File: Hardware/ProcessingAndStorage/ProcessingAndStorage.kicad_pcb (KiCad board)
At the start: 2 copper layers, 85 x 60 mm, 31 parts, among them J1 Micro_SD_Card_Det2, J5 Conn_02x11_Odd_Even, SW2 SW_SPDT_XKB_DMx-xxxx-1, U1 LD1117S50TR_SOT223, U2 ESP-12E, U3 LD1117S50TR_SOT223

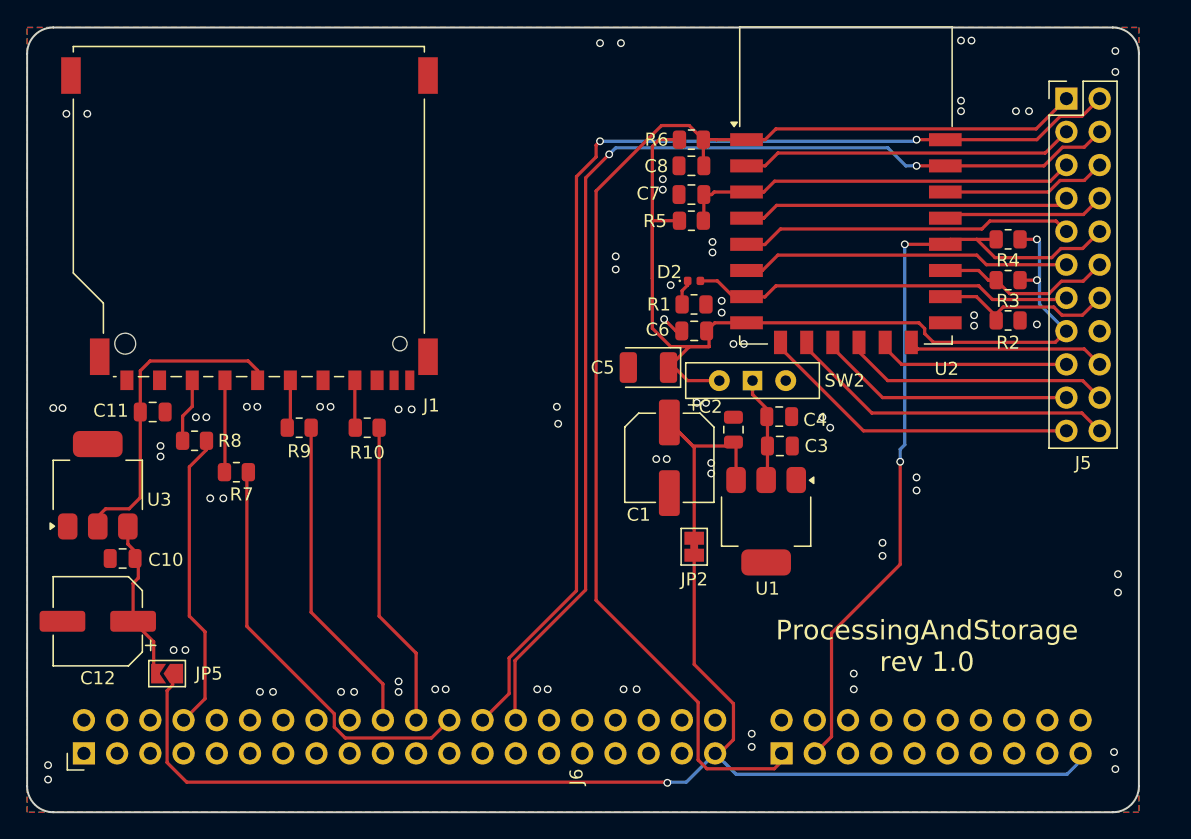
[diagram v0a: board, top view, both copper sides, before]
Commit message: rework CI, make PCB smaller
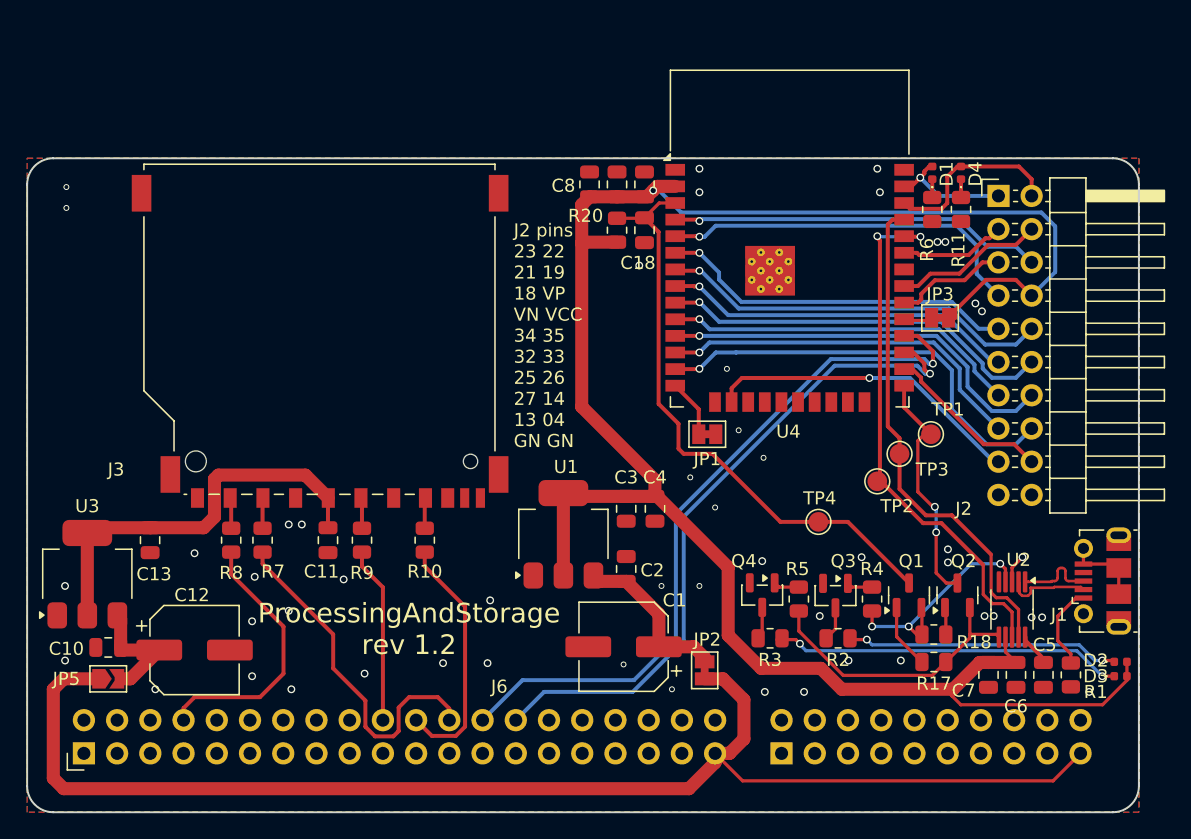
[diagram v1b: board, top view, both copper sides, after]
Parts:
- removed J5: Conn_02x11_Odd_Even, Connector_PinHeader_2.54mm:PinHeader_2x11_P2.54mm_Vertical
- removed SW2: SW_SPDT_XKB_DMx-xxxx-1, Button_Switch_THT:SW_Slide-03_Wuerth-WS-SLTV_10x2.5x6.4_P2.54mm
- added C13: 330n, Capacitor_SMD:C_0805_2012Metric, F.Cu at (139.4, 99.2)
- added C18: 100n, Capacitor_SMD:C_0805_2012Metric, F.Cu at (177.2, 75.5)
- added C20: 100n, Capacitor_SMD:C_0805_2012Metric, F.Cu at (177.2, 72.0)
- added C9: 10u, Capacitor_SMD:C_0805_2012Metric, F.Cu at (175.1, 72.0)
- added D1: LED, LED_SMD:LED_0402_1005Metric, F.Cu at (199.2, 71.1)
- added D3: LED, LED_SMD:LED_0402_1005Metric, F.Cu at (213.6, 109.6)
- added D4: LED, LED_SMD:LED_0402_1005Metric, F.Cu at (201.4, 71.1)
- added J2: Conn_02x10_Odd_Even, Connector_PinHeader_2.54mm:PinHeader_2x10_P2.54mm_Horizontal, F.Cu at (204.3, 72.9)
- added J3: SD_Card_Receptacle, Connector_Card:SD_TE_2041021, F.Cu at (152.4, 84.0)
- added JP1: SolderJumper_2_Bridged, Jumper:SolderJumper-2_P1.3mm_Bridged_Pad1.0x1.5mm, F.Cu at (182.0, 91.1)
- added JP3: SolderJumper_2_Bridged, Jumper:SolderJumper-2_P1.3mm_Bridged_Pad1.0x1.5mm, F.Cu at (199.8, 82.2)
- added Q1: BC846, Package_TO_SOT_SMD:SOT-23, F.Cu at (197.4, 103.4)
- added Q2: BC846, Package_TO_SOT_SMD:SOT-23, F.Cu at (201.1, 103.4)
- added Q3: BC846, Package_TO_SOT_SMD:SOT-23, F.Cu at (191.8, 103.4)
- added Q4: BC846, Package_TO_SOT_SMD:SOT-23, F.Cu at (186.2, 103.4)
- added R11: 1k, Resistor_SMD:R_0805_2012Metric, F.Cu at (201.4, 73.9)
- added R17: 10k, Resistor_SMD:R_0805_2012Metric, F.Cu at (199.3, 108.5)
- added R18: 10k, Resistor_SMD:R_0805_2012Metric, F.Cu at (199.3, 106.4)
- added R20: 10k, Resistor_SMD:R_0805_2012Metric, F.Cu at (175.1, 75.5)
- added TP1: TestPoint, TestPoint:TestPoint_Pad_D1.5mm, F.Cu at (199.1, 91.1)
- added TP2: TestPoint, TestPoint:TestPoint_Pad_D1.5mm, F.Cu at (195.0, 94.7)
- added TP3: TestPoint, TestPoint:TestPoint_Pad_D1.5mm, F.Cu at (196.7, 92.6)
- added TP4: TestPoint, TestPoint:TestPoint_Pad_D1.5mm, F.Cu at (190.5, 97.8)
- added U4: ESP32-WROOM-32E, RF_Module:ESP32-WROOM-32D, F.Cu at (188.3, 79.1)
- C5: value 47u/6V3 -> 100n; footprint Capacitor_Tantalum_SMD:CP_EIA-3528-21_Kemet-B -> Capacitor_SMD:C_0805_2012Metric
- C7: value 100n -> 10u
- C8: value 470p -> 10u
- J1: value Micro_SD_Card_Det2 -> USB_B_Micro; footprint Connector_Card:SD_TE_2041021 -> HardwareDataLogger:USB_Micro-B_Molex-105017-0001_Extra_Mechanical_Pads
- R1: value 470R -> 10k
- R2, R3, R6: value 10k -> 1k
- U1, U3: footprint Package_TO_SOT_SMD:SOT-223 -> Package_TO_SOT_SMD:SOT-223-3_TabPin2
- U2: value ESP-12E -> CH340X; footprint RF_Module:ESP-12E -> Package_SO:MSOP-10_3x3mm_P0.5mm
- moved J1 68.8 mm to (210.0, 102.7), turned to 90 degrees
- moved D2 43.7 mm to (213.6, 108.5)
- moved C7 43.2 mm to (203.5, 109.5), turned to -90 degrees
- moved R1 40.4 mm to (209.8, 109.5), turned to 90 degrees
- moved C5 38.3 mm to (207.7, 109.5), turned to -90 degrees
- moved C6 36.0 mm to (205.6, 109.5), turned to -90 degrees
- moved U2 34.8 mm to (205.3, 104.5), turned to -90 degrees
- moved R3 32.9 mm to (186.8, 106.7)
- moved R5 30.1 mm to (189.0, 103.7), turned to 90 degrees
- moved R4 29.4 mm to (194.6, 103.7), turned to 90 degrees
- moved R2 27.6 mm to (192.0, 106.7), turned to 180 degrees
- moved R6 19.2 mm to (199.2, 73.9), turned to -90 degrees
- moved C11 16.6 mm to (153.0, 99.2), turned to -90 degrees
- moved U1 15.5 mm to (171.0, 98.8), turned to 90 degrees
- moved C1 14.9 mm to (175.6, 107.3), turned to 180 degrees
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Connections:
- C11 pad 1: Net-(J1-VDD) -> Net-(J3-VDD)
- C3 pad 1: 3V3 -> ESP_3V3
- C4 pad 1: 3V3 -> ESP_3V3
- C5 pad 1: ESP_PWR -> Net-(U2-V3)
- C6 pad 1: ESP_PWR -> ESP_3V3
- C7 pad 1: /WiFi/EN -> ESP_3V3
- C8 pad 1: NRST -> ESP_3V3
- D2 pad 2: /WiFi/GPIO13 -> ESP_3V3
- J1 pad 1: unconnected-(J1-DAT2-Pad1) -> Net-(J1-VBUS)
- J1 pad 2: Net-(J1-DAT3/CD) -> /SerialProgrammer/USB_N
- J1 pad 3: Net-(J1-CMD) -> /SerialProgrammer/USB_P
- J1 pad 4: Net-(J1-VDD) -> unconnected-(J1-ID-Pad4)
- J1 pad 5: Net-(J1-CLK) -> GND
- J6 pad 41: NRST -> unconnected-(J6-Pin_41-Pad41)
- J6 pad 43: BOOT0 -> unconnected-(J6-Pin_43-Pad43)
- R1 pad 1: Net-(D2-K) -> GND
- R1 pad 2: GND -> Net-(J1-VBUS)
- R10 pad 2: Net-(J1-DAT0) -> Net-(J3-DAT0)
- R2 pad 1: /WiFi/GPIO15 -> Net-(D2-K)
- R2 pad 2: GND -> Net-(Q3-C)
- R3 pad 1: ESP_PWR -> Net-(D3-K)
- R3 pad 2: /WiFi/GPIO2 -> Net-(Q4-C)
- R4 pad 1: ESP_PWR -> Net-(Q1-E)
- R4 pad 2: BOOT0 -> Net-(Q3-B)
- R5 pad 1: ESP_PWR -> Net-(Q2-E)
- R5 pad 2: /WiFi/EN -> Net-(Q4-B)
- R6 pad 1: ESP_PWR -> Net-(D1-K)
- R6 pad 2: NRST -> GND
- R7 pad 2: Net-(J1-CMD) -> Net-(J3-CMD)
- R8 pad 2: Net-(J1-DAT3/CD) -> Net-(J3-CD/DAT3)
- R9 pad 2: Net-(J1-CLK) -> Net-(J3-CLK)
- U1 pad 2: 3V3 -> ESP_3V3
- U2 pad 1: NRST -> /SerialProgrammer/USB_P
- U2 pad 10: /WiFi/ESP32_MISO -> Net-(U2-V3)
- U2 pad 2: /WiFi/ESP_ADC -> /SerialProgrammer/USB_N
- U2 pad 3: /WiFi/EN -> GND
- U2 pad 4: /WiFi/GPIO16 -> Net-(Q1-E)
- U2 pad 5: /WiFi/GPIO14 -> unconnected-(U2-~{CTS}-Pad5)
- U2 pad 6: /WiFi/GPIO12 -> Net-(Q2-E)
- U2 pad 7: /WiFi/GPIO13 -> ESP_3V3
- U2 pad 8: ESP_PWR -> ESP_U0_TX
- U2 pad 9: /WiFi/ESP32_CS0 -> ESP_U0_RX
- U3 pad 2: Net-(J1-VDD) -> Net-(J3-VDD)
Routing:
- net ESP_3V3: track 0.00 -> 153.0 mm, vias 0 -> 1
- net NRST: track 95.4 -> 0.00 mm
- net ESP_PWR: track 75.6 -> 0.00 mm, vias 2 -> 0
- net BOOT0: track 59.7 -> 0.00 mm, vias 2 -> 0
- net ESP_EN: track 0.00 -> 45.5 mm
- net ESP_U0_TX: track 0.00 -> 40.5 mm, vias 0 -> 2
- net ESP_U0_RX: track 0.00 -> 38.7 mm
- net USART1_TX: track 85.5 -> 51.6 mm, vias 2 -> 1
- net /WiFi/IO14: track 0.00 -> 32.7 mm, vias 0 -> 1
- net USART1_RX: track 87.5 -> 55.2 mm, vias 2 -> 1
- net /WiFi/IO26: track 0.00 -> 31.0 mm, vias 0 -> 1
- net Net-(J3-VDD): track 0.00 -> 30.7 mm
- net /WiFi/EN: track 30.6 -> 0.00 mm
- net /WiFi/IO33: track 0.00 -> 30.2 mm, vias 0 -> 1
- net /WiFi/IO35: track 0.00 -> 30.0 mm, vias 0 -> 1
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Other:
- board size 85 x 60 mm -> 85 x 50 mm
- board text added: "J2 pins 23 22 21 19 18 VP VN VCC 34 35 32 33 25 26 27 14 13 04 GN GN"
- board text added: "ProcessingAndStorage rev 1.2"
- board text removed: "ProcessingAndStorage rev 1.0"
